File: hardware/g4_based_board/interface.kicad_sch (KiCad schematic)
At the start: 26 parts, among them J1 USB_C_Receptacle_USB2.0, J2 Micro_SD_Card_Det1, Q1 NPN, Q2 NPN

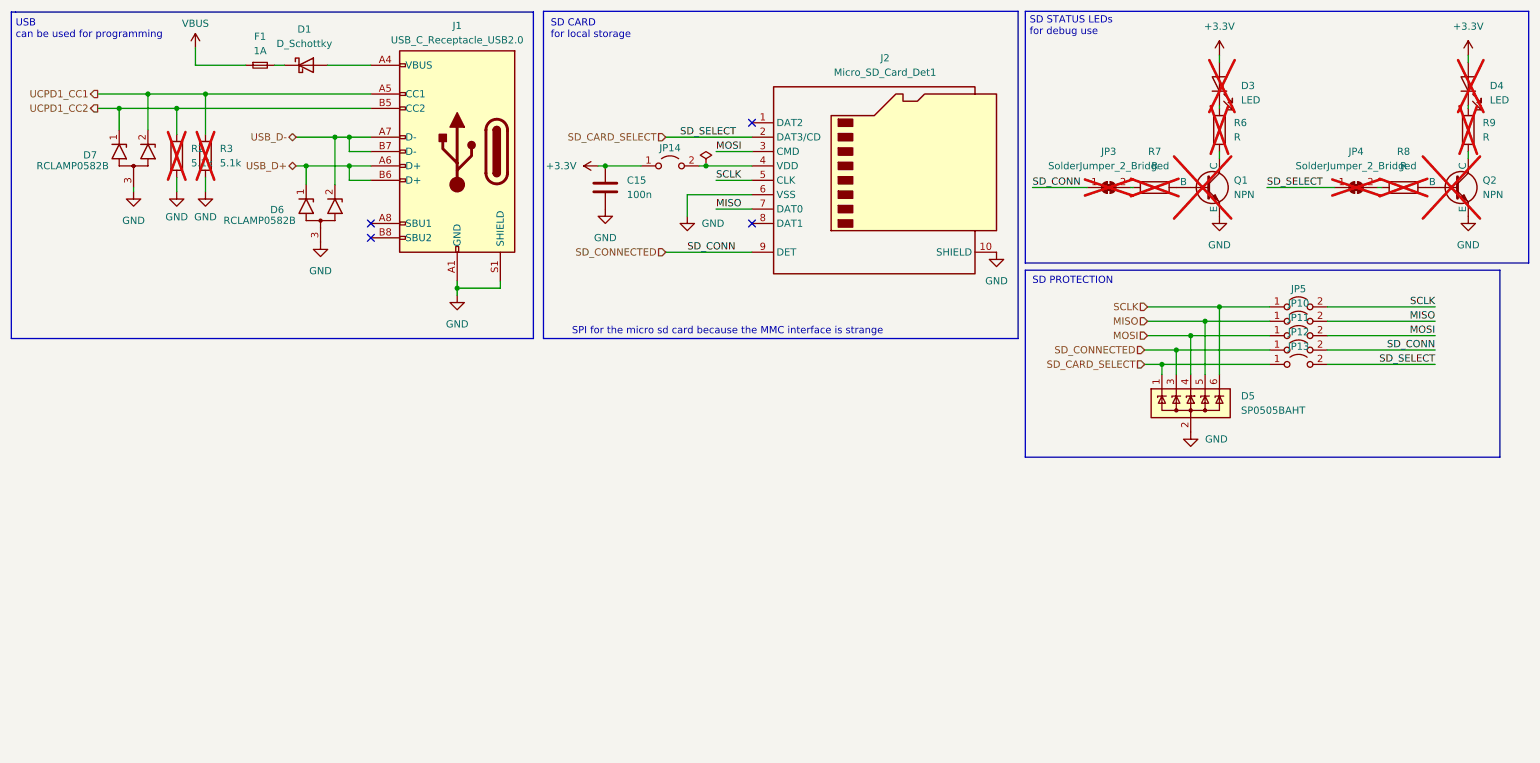
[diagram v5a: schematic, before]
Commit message: fix some erc violations
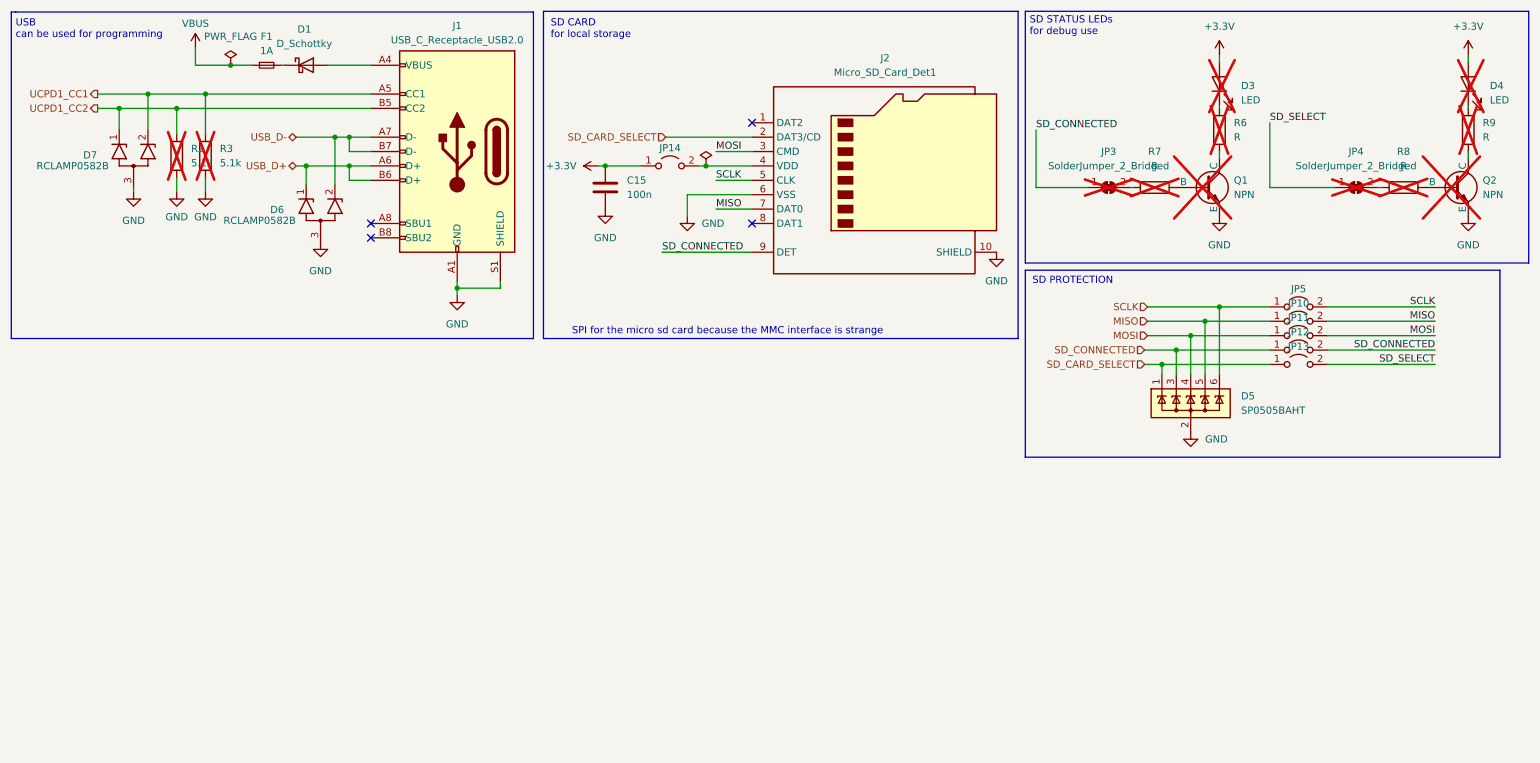
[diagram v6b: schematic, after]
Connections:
- net SD_CARD_SELECT: no longer JP13.2 (B), JP4.1 (A)
- new net SD_SELECT: JP13.2 (B), JP4.1 (A)
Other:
- moved on the sheet: F1
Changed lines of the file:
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@@
 	)
 	(junction
+		(at 53.975 24.13)
+		(diameter 0)
+		(color 0 0 0 0)
+	)
+	(junction
 		(at 226.06 69.342)
 		(diameter 0)
@@
 	(wire
 		(pts
+			(xy 196.215 45.72) (xy 205.232 45.72)
+		)
+		(stroke
+			(width 0)
+			(type default)
+		)
+	)
+	(wire
+		(pts
 			(xy 215.392 76.962) (xy 218.44 76.962)
 		)
@@
 	(wire
 		(pts
+			(xy 196.215 35.56) (xy 196.215 45.72)
+		)
+		(stroke
+			(width 0)
+			(type default)
+		)
+	)
+	(wire
+		(pts
 			(xy 93.98 63.5) (xy 93.98 64.77)
 		)
@@
 	(wire
 		(pts
-			(xy 247.65 69.342) (xy 266.7 69.342)
+			(xy 237.49 45.72) (xy 248.92 45.72)
 		)
 		(stroke
@@
 	(wire
 		(pts
-			(xy 220.98 74.422) (xy 215.392 74.422)
+			(xy 247.65 69.342) (xy 266.7 69.342)
 		)
 		(stroke
@@
 	(wire
 		(pts
-			(xy 226.06 69.342) (xy 237.49 69.342)
+			(xy 220.98 74.422) (xy 215.392 74.422)
 		)
 		(stroke
@@
 	(wire
 		(pts
-			(xy 74.93 41.91) (xy 74.93 44.45)
+			(xy 226.06 69.342) (xy 237.49 69.342)
 		)
 		(stroke
@@
 	(wire
 		(pts
-			(xy 218.44 76.962) (xy 218.44 78.74)
+			(xy 74.93 41.91) (xy 74.93 44.45)
 		)
 		(stroke
@@
 	(wire
 		(pts
-			(xy 101.6 62.23) (xy 101.6 63.5)
+			(xy 218.44 76.962) (xy 218.44 78.74)
 		)
 		(stroke
@@
 	(wire
 		(pts
-			(xy 247.65 66.802) (xy 266.7 66.802)
+			(xy 101.6 62.23) (xy 101.6 63.5)
 		)
 		(stroke
@@
 	(wire
 		(pts
-			(xy 228.6 66.802) (xy 237.49 66.802)
+			(xy 247.65 66.802) (xy 266.7 66.802)
 		)
 		(stroke
@@
 	(wire
 		(pts
-			(xy 130.81 57.15) (xy 146.05 57.15)
+			(xy 228.6 66.802) (xy 237.49 66.802)
 		)
 		(stroke
@@
 	(wire
 		(pts
-			(xy 236.982 45.72) (xy 248.92 45.72)
-		)
-		(stroke
-			(width 0)
-			(type default)
-		)
-	)
-	(wire
-		(pts
 			(xy 65.532 41.91) (xy 67.31 41.91)
 		)
@@
 	(wire
 		(pts
+			(xy 53.975 24.13) (xy 47.752 24.13)
+		)
+		(stroke
+			(width 0)
+			(type default)
+		)
+	)
+	(wire
+		(pts
 			(xy 136.652 41.91) (xy 137.922 41.91)
 		)
@@
 	(wire
 		(pts
+			(xy 237.49 34.29) (xy 237.49 45.72)
+		)
+		(stroke
+			(width 0)
+			(type default)
+		)
+	)
+	(wire
+		(pts
 			(xy 67.31 41.91) (xy 74.93 41.91)
 		)
@@
 	(wire
 		(pts
-			(xy 61.722 24.13) (xy 63.5 24.13)
+			(xy 62.865 24.13) (xy 63.5 24.13)
 		)
 		(stroke
@@
 	(wire
 		(pts
-			(xy 56.642 24.13) (xy 47.752 24.13)
+			(xy 57.785 24.13) (xy 53.975 24.13)
 		)
 		(stroke
@@
 	(wire
 		(pts
-			(xy 195.58 45.72) (xy 205.232 45.72)
-		)
-		(stroke
-			(width 0)
-			(type default)
-		)
-	)
-	(wire
-		(pts
 			(xy 272.542 31.242) (xy 272.542 31.75)
 		)
@@
 		)
 	)
+	(wire
+		(pts
+			(xy 130.175 57.15) (xy 146.05 57.15)
+		)
+		(stroke
+			(width 0)
+			(type default)
+		)
+	)
 	(rectangle
 		(start 109.22 14.605)
@@
 	)
 	(label "SD_SELECT"
-		(at 236.982 45.72 0)
+		(at 237.49 34.29 0)
 		(fields_autoplaced yes)
 		(effects
@@
 		)
 	)
-	(label "SD_CONN"
-		(at 134.62 57.15 0)
+	(label "SD_CONNECTED"
+		(at 130.175 57.15 0)
 		(fields_autoplaced yes)
 		(effects
@@
 		)
 	)
-	(label "SD_CONN"
+	(label "SD_CONNECTED"
 		(at 266.7 74.422 180)
 		(fields_autoplaced yes)
@@
 		)
 	)
-	(label "SD_CONN"
-		(at 195.58 45.72 0)
+	(label "SD_CONNECTED"
+		(at 196.215 35.56 0)
 		(fields_autoplaced yes)
 		(effects
@@
 		)
 	)
-	(label "SD_SELECT"
-		(at 133.35 36.83 0)
-		(fields_autoplaced yes)
-		(effects
-			(font
-				(size 1.27 1.27)
-			)
-			(justify left bottom)
-		)
-	)
 	(label "MISO"
 		(at 266.7 69.342 180)
@@
 		)
 	)
-	(hierarchical_label "SD_CONNECTED"
-		(shape input)
-		(at 130.81 57.15 180)
-		(fields_autoplaced yes)
-		(effects
-			(font
-				(size 1.27 1.27)
-			)
-			(justify right)
-		)
-	)
 	(symbol
 		(lib_id "power:+3.3V")
@@
 	)
 	(symbol
+		(lib_id "power:PWR_FLAG")
+		(at 53.975 24.13 0)
+		(unit 1)
+		(exclude_from_sim no)
+		(in_bom yes)
+		(on_board yes)
+		(dnp no)
+		(fields_autoplaced yes)
+		(property "Reference" "#FLG029"
+			(at 53.975 22.225 0)
+			(effects
+				(font
+					(size 1.27 1.27)
+				)
+				(hide yes)
+			)
+		)
+		(property "Value" "PWR_FLAG"
+			(at 53.975 19.05 0)
+			(effects
+				(font
+					(size 1.27 1.27)
+				)
+			)
+		)
+		(property "Footprint" ""
+			(at 53.975 24.13 0)
+			(effects
+				(font
+					(size 1.27 1.27)
+				)
+				(hide yes)
+			)
+		)
+		(property "Datasheet" "~"
+			(at 53.975 24.13 0)
+			(effects
+				(font
+					(size 1.27 1.27)
+				)
+				(hide yes)
+			)
+		)
+		(property "Description" "Special symbol for telling ERC where power comes from"
+			(at 53.975 24.13 0)
+			(effects
+				(font
+					(size 1.27 1.27)
+				)
+				(hide yes)
+			)
+		)
+		(pin "1"
+		)
+		(instances
+			(project "data_logger"
+				(path "/9bc93932-ff5f-4f35-96cf-dfa5f042acb6/b63f81bc-3201-4d22-bdc3-2e8eb19f6492"
+					(reference "#FLG029")
+					(unit 1)
+				)
+			)
+		)
+	)
+	(symbol
 		(lib_id "power:GND")
 		(at 44.45 46.482 0)
@@
 	(symbol
 		(lib_id "Device:Fuse_Small")
-		(at 59.182 24.13 0)
+		(at 60.325 24.13 0)
 		(unit 1)
 		(exclude_from_sim no)
@@
 		(fields_autoplaced yes)
 		(property "Reference" "F1"
-			(at 59.182 19.05 0)
+			(at 60.325 19.05 0)
 			(effects
 				(font
@@
 		)
 		(property "Value" "1A"
-			(at 59.182 21.59 0)
+			(at 60.325 21.59 0)
 			(effects
 				(font
@@
 		)
 		(property "Footprint" "Fuse:Fuse_0805_2012Metric_Pad1.15x1.40mm_HandSolder"
-			(at 59.182 24.13 0)
+			(at 60.325 24.13 0)
 			(effects
 				(font
@@
 		)
 		(property "Datasheet" "~"
-			(at 59.182 24.13 0)
+			(at 60.325 24.13 0)
 			(effects
 				(font
@@
 		)
 		(property "Description" "Fuse, small symbol"
-			(at 59.182 24.13 0)
+			(at 60.325 24.13 0)
 			(effects
 				(font

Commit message: added an extra tvs diodes to both 3.3v and sd_conn on the sd card
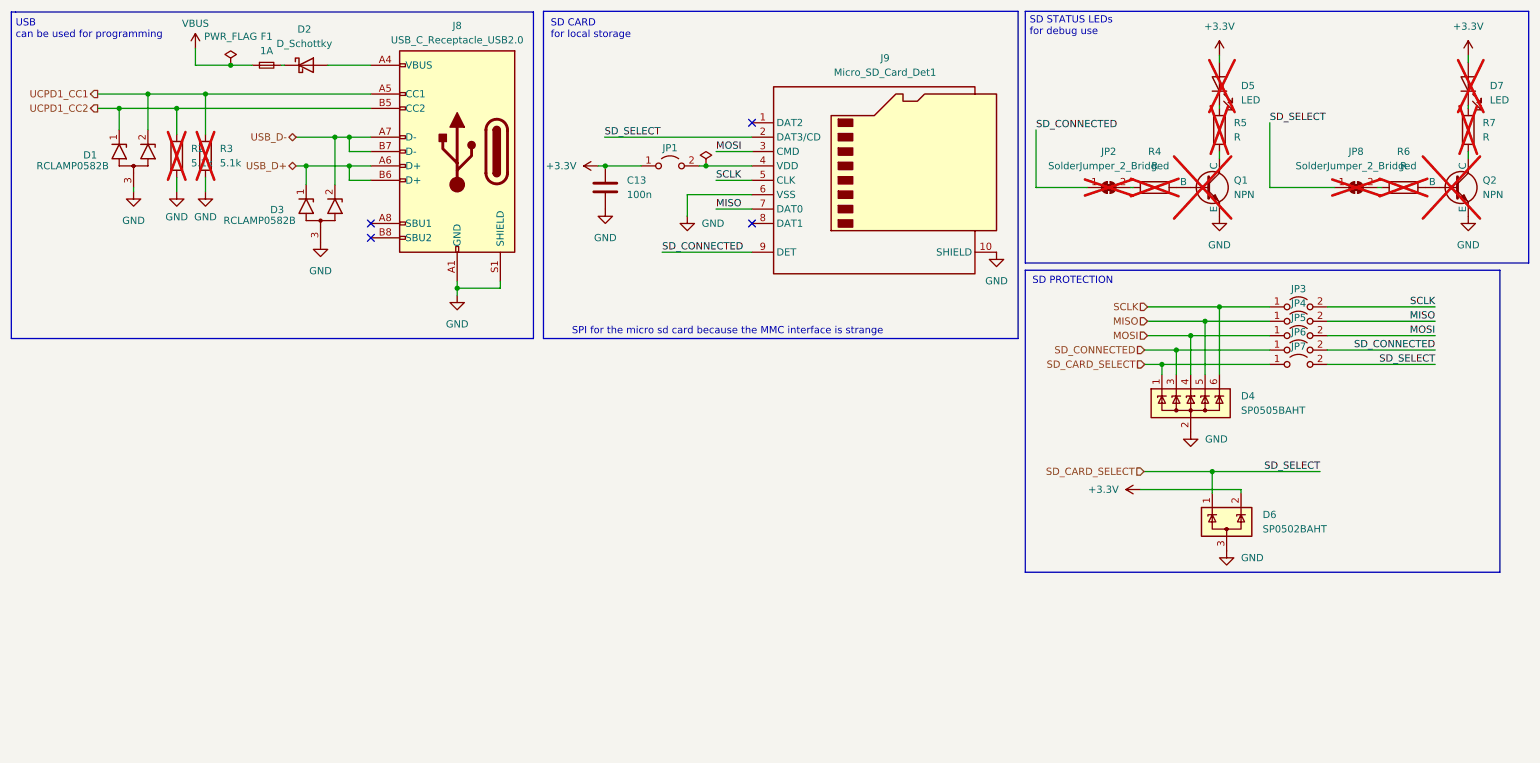
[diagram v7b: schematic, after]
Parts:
- added D6: SP0502BAHT, Package_TO_SOT_SMD:SOT-23, symbol Power_Protection:SP0502BAHT
- renumbered C15 to C13, D7 to D1, D1 to D2, D6 to D3, D5 to D4, D3 to D5, D4 to D7, J1 to J8, J2 to J9, JP14 to JP1, JP3 to JP2, JP5 to JP3, JP10 to JP4, JP11 to JP5, JP12 to JP6, JP13 to JP7, JP4 to JP8, R7 to R4, R6 to R5, R8 to R6, R9 to R7
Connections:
- net SD_SELECT is gone; now on net SD_CARD_SELECT: JP7.2 (B), JP8.1 (A)
- net +3.3V: now also D6.2 (K)
- net GND: now also D6.3 (A)
- net SD_CARD_SELECT: now also D6.1 (K)

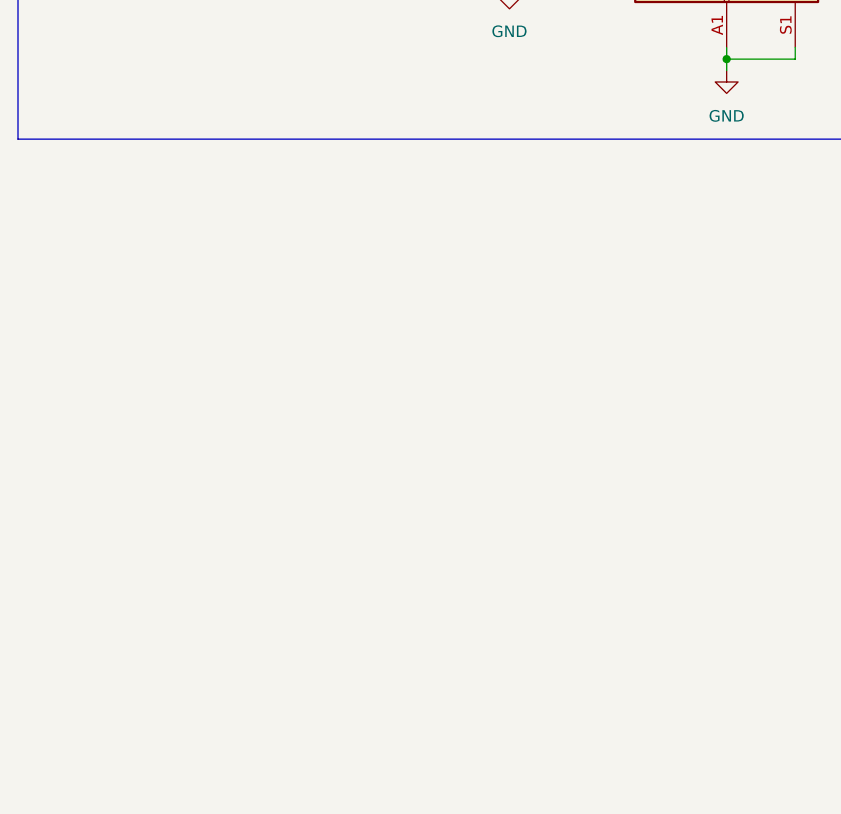
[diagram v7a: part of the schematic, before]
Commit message: added buttons for interfacing with the mcu
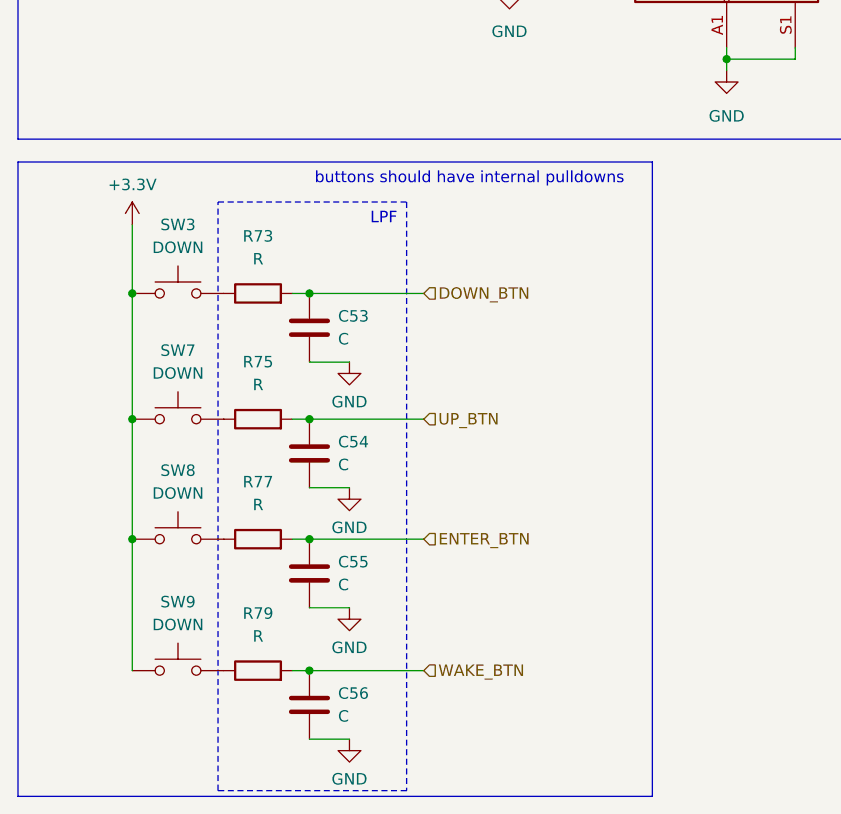
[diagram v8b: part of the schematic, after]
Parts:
- added C53, C54, C55, C56: C, Capacitor_SMD:C_0603_1608Metric_Pad1.08x0.95mm_HandSolder, symbol Device:C
- added R73, R75, R77, R79: R, Resistor_SMD:R_0603_1608Metric_Pad0.98x0.95mm_HandSolder, symbol Device:R
- added SW3, SW7, SW8, SW9: DOWN, Button_Switch_THT:SW_TH_Tactile_Omron_B3F-10xx, symbol Switch:SW_Push
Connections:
- net +3.3V: now also SW3.1, SW7.1, SW8.1, SW9.1
- net GND: now also C53.2, C54.2, C55.2, C56.2
- new net: R73.1, SW3.2
- new net: R79.1, SW9.2
- new net: R75.1, SW7.2
- new net: R77.1, SW8.2
- new net DOWN_BTN: C53.1, R73.2
- new net ENTER_BTN: C55.1, R77.2
- new net UP_BTN: C54.1, R75.2
- new net WAKE_BTN: C56.1, R79.2
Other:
- note added: "LPF"
- note added: "buttons should have internal pulldowns"
